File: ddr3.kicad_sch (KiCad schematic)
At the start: 29 parts, among them U11 LIFCL-40-9BG256C, U12 MT41K128M16JT-125_K

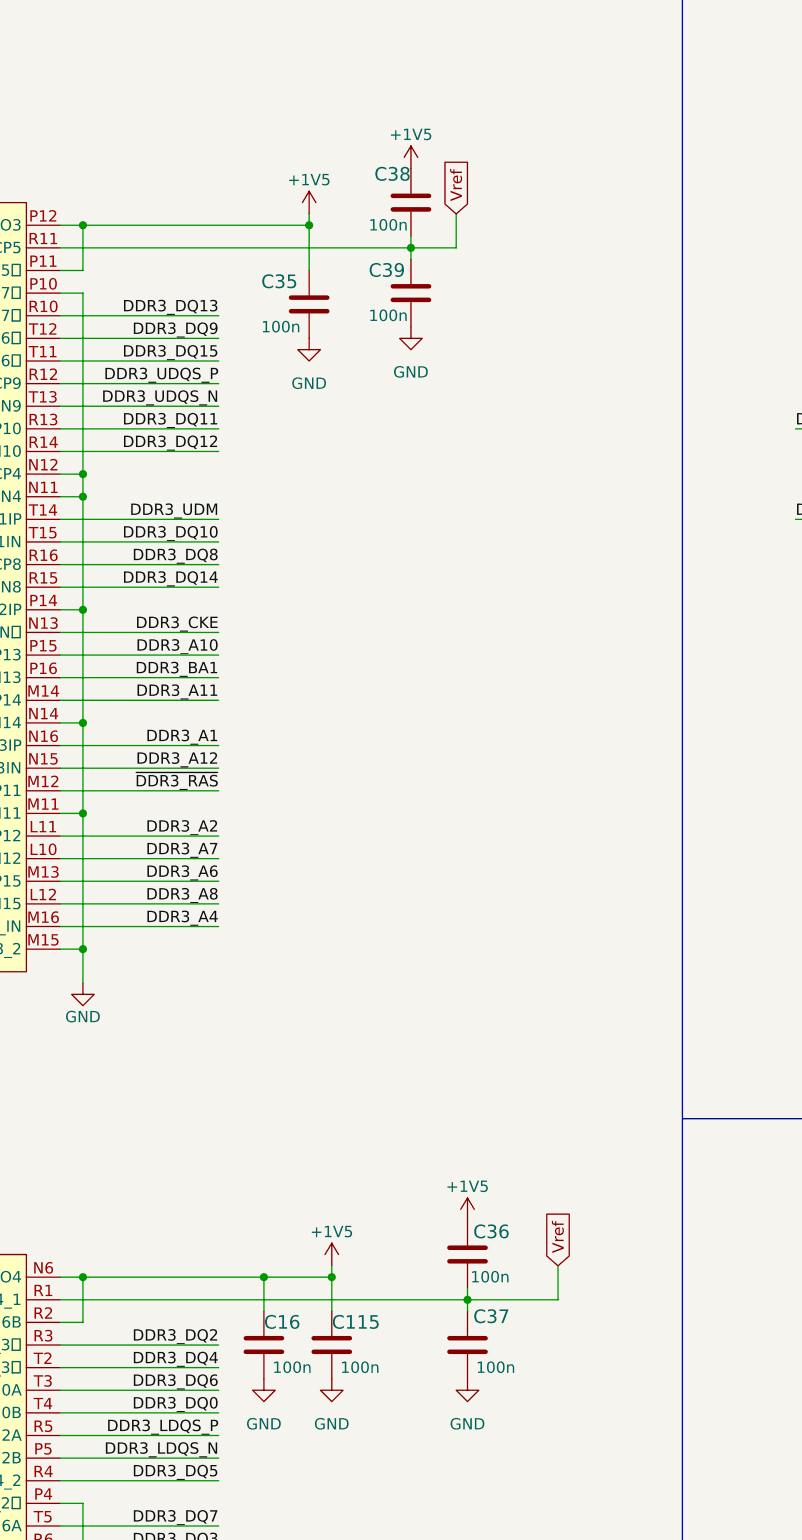
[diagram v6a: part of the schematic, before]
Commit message: Update PCB routing
- apply new DRC
- add FPGA package delay to the high speed traces tunning
- improve GND and power planes
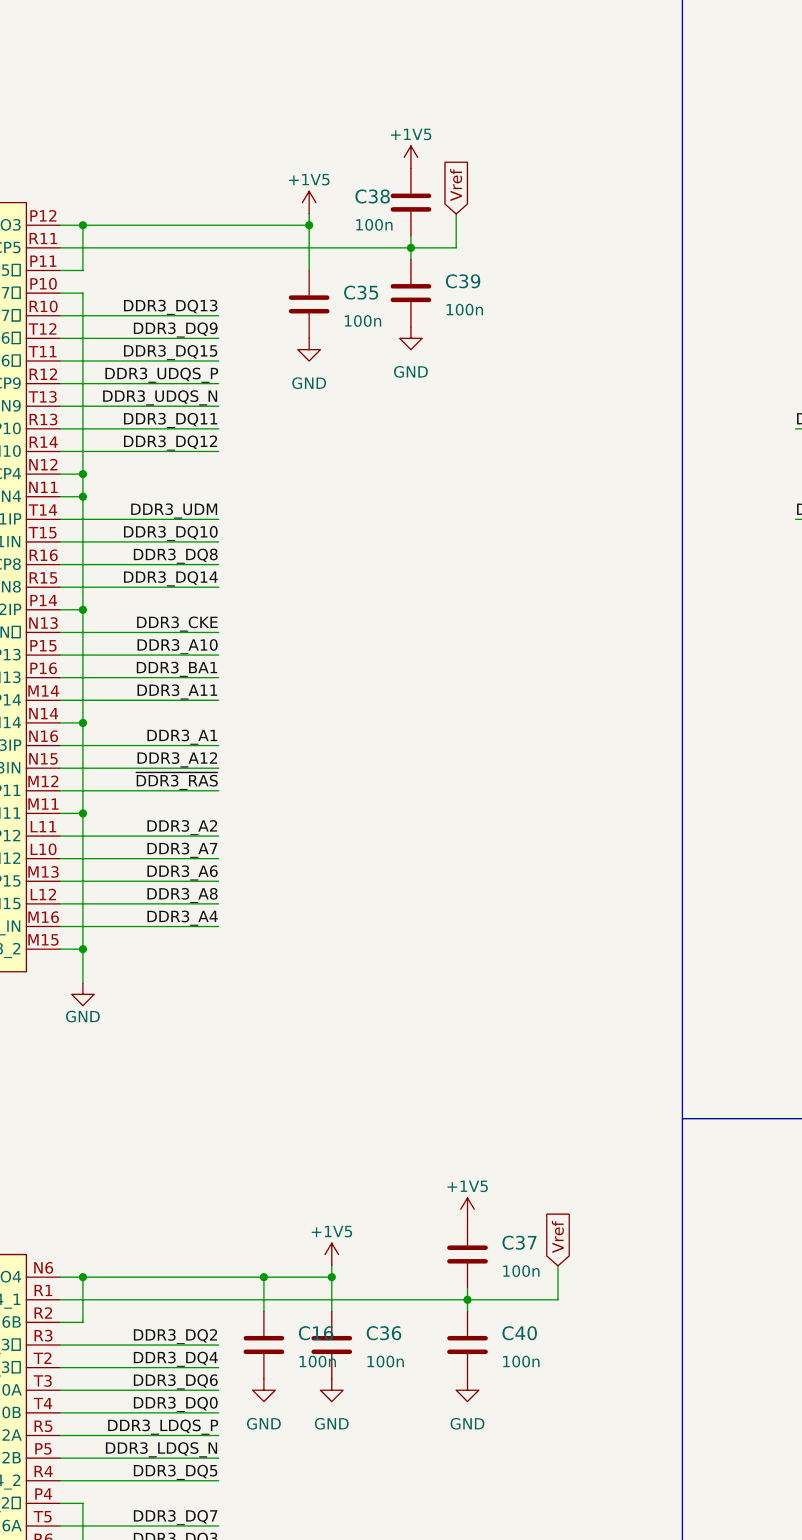
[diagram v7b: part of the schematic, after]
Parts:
- removed C115, C16, C35, C36, C37, C38, C39: C_100n_0402, crosslink-nx-video-converter-footprints:0402-cap, symbol crosslink-nx-video-converter:C_100n_0402
- added C16, C35, C36, C37, C38, C39, C40: C_100n_0201, crosslink-nx-video-converter-footprints:0201-res, symbol crosslink-nx-video-converter:C_100n_0201
- U11: footprint crosslink-nx-video-converter-footprints:BGA-256_16x16_14.0x14.0mm -> crosslink-nx-video-converter-footprints:CrosslinkNX-BGA-256_16x16_14.0x14.0mm
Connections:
- net +1V5: now also C16.1, C35.1, C36.1, C37.1, C38.1
- net GND: now also C16.2, C35.2, C36.2, C39.2, C40.2
- net Vref: now also C37.2, C38.2, C39.1, C40.1

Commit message: Update project naming convention
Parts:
- C119, C120, C41, C42, C43, C44, C45, C46, C47, C48, C49, C50: footprint crosslink-nx-video-converter-footprints:0402-cap -> sdi-mipi-cross-converter-footprints:0402-cap; symbol crosslink-nx-video-converter:C_100n_0402 -> sdi-mipi-cross-converter:C_100n_0402
- C16, C35, C36, C37, C38, C39, C40: footprint crosslink-nx-video-converter-footprints:0201-res -> sdi-mipi-cross-converter-footprints:0201-res; symbol crosslink-nx-video-converter:C_100n_0201 -> sdi-mipi-cross-converter:C_100n_0201
- R43: footprint crosslink-nx-video-converter-footprints:0201-res -> sdi-mipi-cross-converter-footprints:0201-res; symbol crosslink-nx-video-converter:R_100R_0201 -> sdi-mipi-cross-converter:R_100R_0201
- R44, R45, R46, R48, R49, R50: footprint crosslink-nx-video-converter-footprints:R_Array_4x0402 -> sdi-mipi-cross-converter-footprints:R_Array_4x0402; symbol crosslink-nx-video-converter:4x51R_0402_array -> sdi-mipi-cross-converter:4x51R_0402_array
- R47: footprint crosslink-nx-video-converter-footprints:0402-res -> sdi-mipi-cross-converter-footprints:0402-res; symbol crosslink-nx-video-converter:R_240R_1%_0402 -> sdi-mipi-cross-converter:R_240R_1%_0402
- U11: footprint crosslink-nx-video-converter-footprints:CrosslinkNX-BGA-256_16x16_14.0x14.0mm -> sdi-mipi-cross-converter-footprints:CrosslinkNX-BGA-256_16x16_14.0x14.0mm; symbol crosslink-nx-video-converter:LIFCL-40-9BG256C -> sdi-mipi-cross-converter:LIFCL-40-9BG256C
- U12: footprint crosslink-nx-video-converter-footprints:BGA80P96C6X16_800X1400X110 -> sdi-mipi-cross-converter-footprints:BGA80P96C6X16_800X1400X110; symbol crosslink-nx-video-converter:MT41K128M16JT-125_K -> sdi-mipi-cross-converter:MT41K128M16JT-125_K
